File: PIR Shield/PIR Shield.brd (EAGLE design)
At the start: 68.6 x 53.3 mm, 12 parts, among them IC1 MC33269T-5.0, J1 POWER_JACKPTH

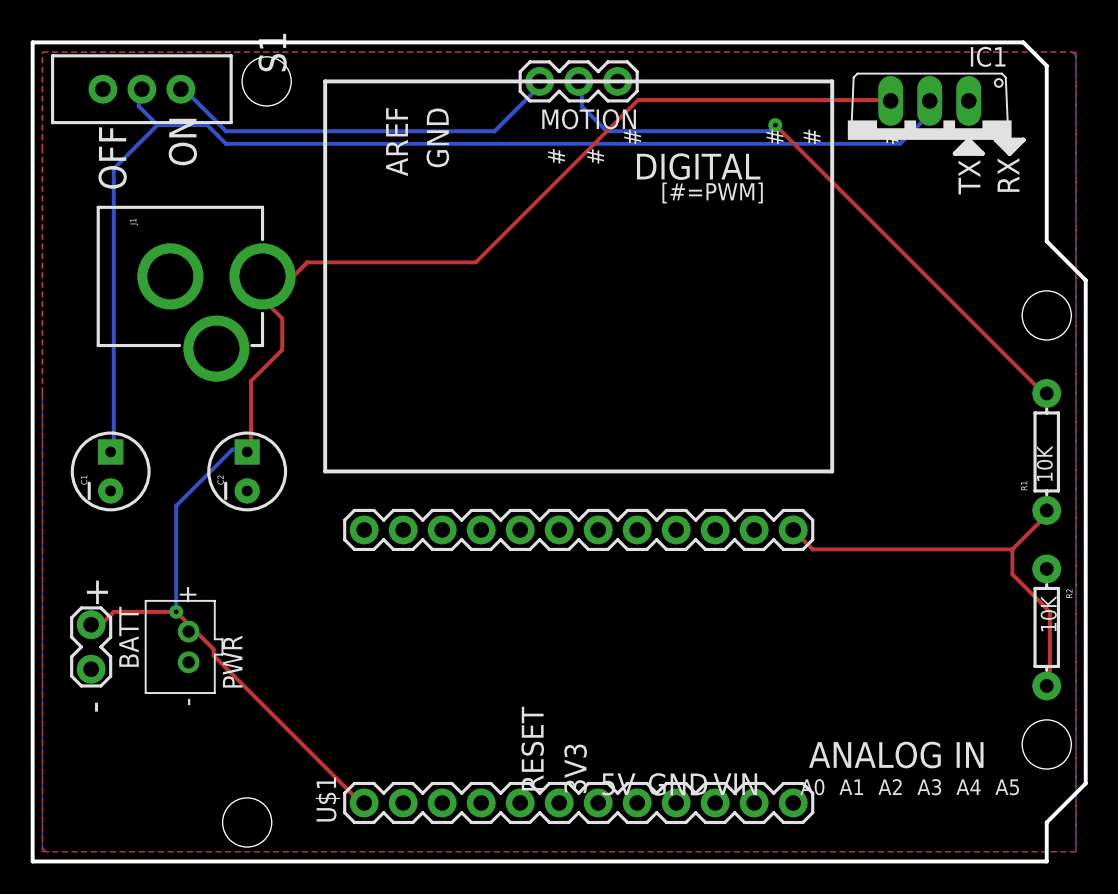
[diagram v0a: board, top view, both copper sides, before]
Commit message: Reviewed battery shield and PIR shield. Good to go.
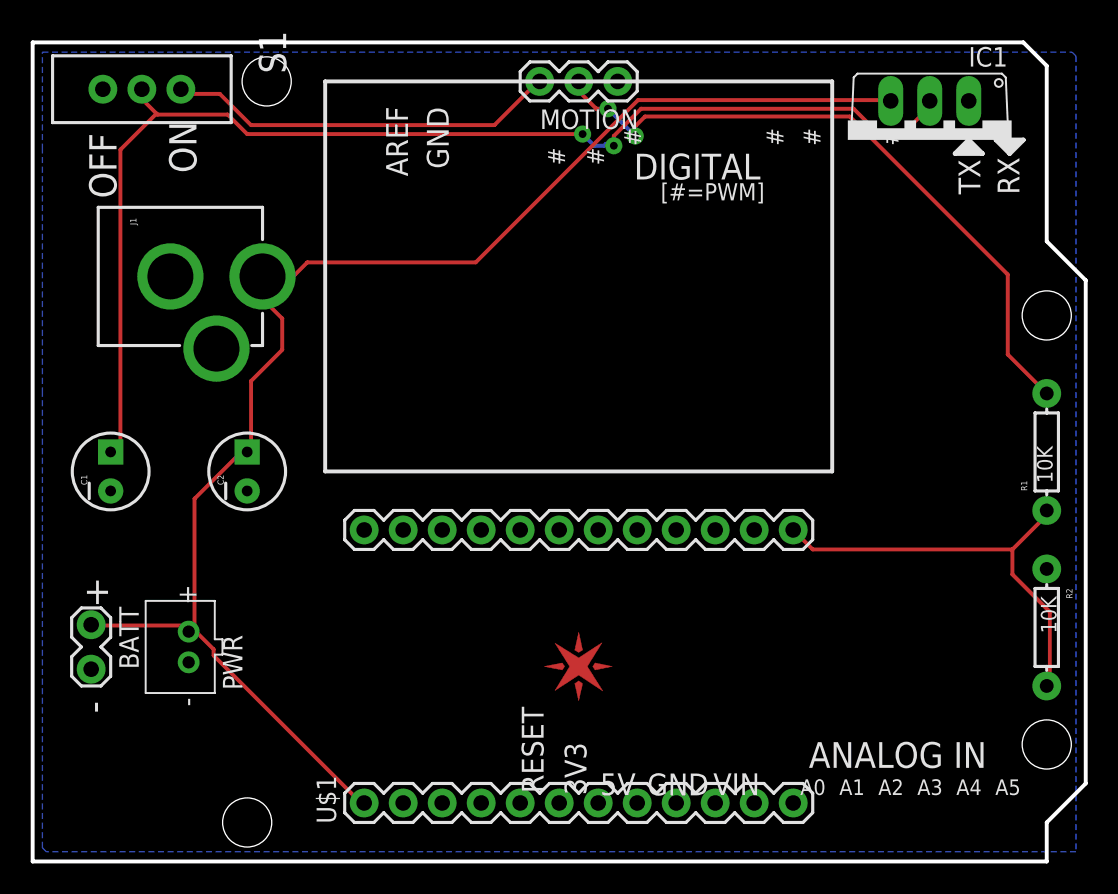
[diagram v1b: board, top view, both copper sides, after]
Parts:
- added U$3: (no value), Spark:SPARK_LOGO_PLUS_PLANE
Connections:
- net VIN renamed VCC
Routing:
- net OUT: track 40.2 -> 43.7 mm, vias 1 -> 2
- net N1: track 77.9 -> 79.9 mm, vias 0 -> 2
- net VCC: track 96.6 -> 95.6 mm, vias 1 -> 0
- net +5V: track 26.6 -> 25.6 mm
- removed copper zone on layer 1, net GND
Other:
- board text added: "Spark PIR Shield v0.1 2013-04-05"
